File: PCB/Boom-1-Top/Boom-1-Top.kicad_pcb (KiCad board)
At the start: 2 copper layers, 345 x 165 mm, 493 parts, among them J1 DEBUG, J10 MCLRCap, J10 PIC_DEBUG, J11 MCLRCap, J11 PIC_DEBUG, J12 MCLRCap, J12 PIC_DEBUG, J13 MCLRCap, J13 PIC_DEBUG, J14 MCLRCap, J14 PIC_DEBUG, J2 MIDI IN, J3 MIDI OUT, J37 Osc1Conn, J38 Osc2Conn, J39 SubNoiseConn, J4 MCLRCap, J4 PIC_DEBUG, J40 FiltConn2, J41 EnvGenConn2, J42 EnvGenConn1, J43 FXConn1, J44 FiltConn1, J45 FXConn2, J46 EnvGenConn3, J5 MCLRCap, J5 PIC_DEBUG, J6 MCLRCap, J6 PIC_DEBUG, J7 MCLRCap, J7 PIC_DEBUG, J8 MCLRCap, J8 PIC_DEBUG, J9 MCLRCap, J9 PIC_DEBUG, SW1 Rotary_Encoder, SW10 Rotary_Encoder, SW11 Rotary_Encoder, SW12 Rotary_Encoder, SW13 Rotary_Encoder, SW14 Rotary_Encoder, SW15 Rotary_Encoder_Switch, SW16 Rotary_Encoder_Switch, SW17 Rotary_Encoder, SW18 Rotary_Encoder, SW19 Rotary_Encoder, SW2 Rotary_Encoder, SW20 Rotary_Encoder, SW21 Rotary_Encoder, SW22 Rotary_Encoder, SW23 Rotary_Encoder, SW24 Rotary_Encoder, SW25 Rotary_Encoder, SW26 Rotary_Encoder, SW27 Rotary_Encoder, SW28 Rotary_Encoder_Switch, SW29 Rotary_Encoder, SW3 Rotary_Encoder, SW30 Rotary_Encoder, SW31 Rotary_Encoder, SW32 Rotary_Encoder, SW33 Rotary_Encoder, SW34 Rotary_Encoder, SW35 Rotary_Encoder, SW36 Rotary_Encoder, SW37 Rotary_Encoder, SW38 Rotary_Encoder, SW39 Rotary_Encoder, SW4 Rotary_Encoder, SW40 Rotary_Encoder, SW41 Reset, SW42 Reset, SW43 Reset, SW44 Reset, SW45 Reset, SW46 Reset, SW47 Reset, SW48 Reset, SW49 Reset, SW5 Rotary_Encoder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

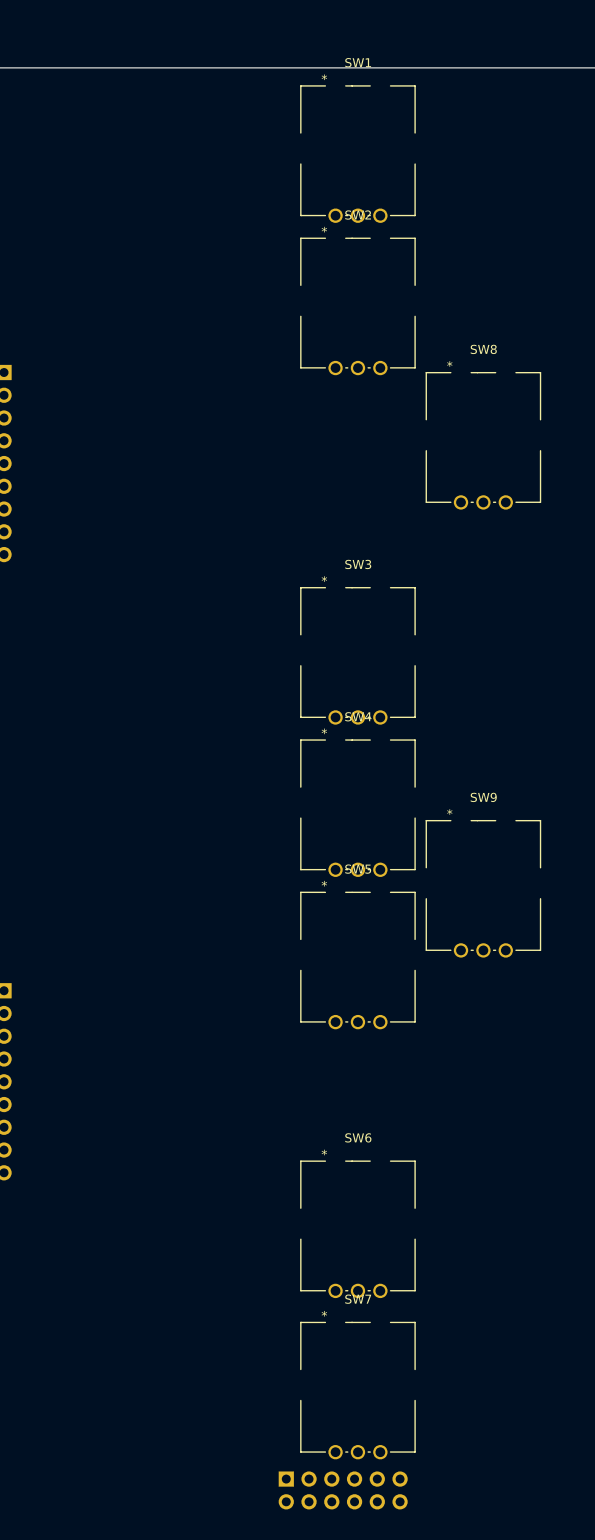
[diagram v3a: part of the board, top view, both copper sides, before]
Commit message: locked headers
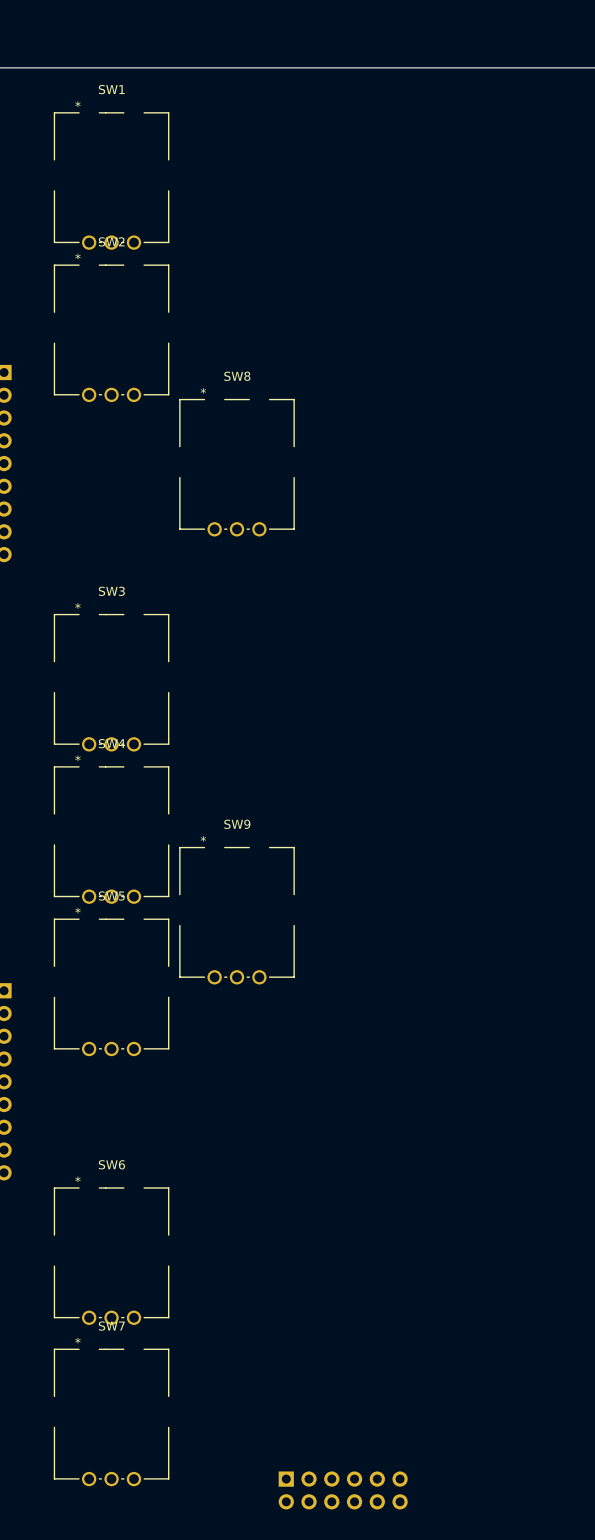
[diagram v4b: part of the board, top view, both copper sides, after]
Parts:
- moved SW1 27.7 mm to (48.5, 35.0)
- moved SW2 27.7 mm to (48.5, 52.0)
- moved SW3 27.7 mm to (48.5, 91.0)
- moved SW4 27.7 mm to (48.5, 108.0)
- moved SW5 27.7 mm to (48.5, 125.0)
- moved SW6 27.7 mm to (48.5, 155.0)
- moved SW7 27.7 mm to (48.5, 173.0)
- moved SW8 27.7 mm to (62.5, 67.0)
- moved SW9 27.7 mm to (62.5, 117.0)
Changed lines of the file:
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@@
   )
   (module PEC11R:PEC11R-4x15F-N0024 (layer F.Cu)
-    (at 90 114)
+    (at 62.5 117)
     (fp_text reference SW9 (at 2.54 -2.54) (layer F.SilkS)
       (effects (font (size 1 1) (thickness 0.15)))
@@
   )
   (module PEC11R:PEC11R-4x15F-N0024 (layer F.Cu)
-    (at 90 64)
+    (at 62.5 67)
     (fp_text reference SW8 (at 2.54 -2.54) (layer F.SilkS)
       (effects (font (size 1 1) (thickness 0.15)))
@@
   )
   (module PEC11R:PEC11R-4x15F-N0024 (layer F.Cu)
-    (at 76 170)
+    (at 48.5 173)
     (fp_text reference SW7 (at 2.54 -2.54) (layer F.SilkS)
       (effects (font (size 1 1) (thickness 0.15)))
@@
   )
   (module PEC11R:PEC11R-4x15F-N0024 (layer F.Cu)
-    (at 76 152)
+    (at 48.5 155)
     (fp_text reference SW6 (at 2.54 -2.54) (layer F.SilkS)
       (effects (font (size 1 1) (thickness 0.15)))
@@
   )
   (module PEC11R:PEC11R-4x15F-N0024 (layer F.Cu)
-    (at 76 122)
+    (at 48.5 125)
     (fp_text reference SW5 (at 2.54 -2.54) (layer F.SilkS)
       (effects (font (size 1 1) (thickness 0.15)))
@@
   )
   (module PEC11R:PEC11R-4x15F-N0024 (layer F.Cu)
-    (at 76 105)
+    (at 48.5 108)
     (fp_text reference SW4 (at 2.54 -2.54) (layer F.SilkS)
       (effects (font (size 1 1) (thickness 0.15)))
@@
   )
   (module PEC11R:PEC11R-4x15F-N0024 (layer F.Cu)
-    (at 76 88)
+    (at 48.5 91)
     (fp_text reference SW3 (at 2.54 -2.54) (layer F.SilkS)
       (effects (font (size 1 1) (thickness 0.15)))
@@
   )
   (module PEC11R:PEC11R-4x15F-N0024 (layer F.Cu)
-    (at 76 49)
+    (at 48.5 52)
     (fp_text reference SW2 (at 2.54 -2.54) (layer F.SilkS)
       (effects (font (size 1 1) (thickness 0.15)))
@@
   )
   (module PEC11R:PEC11R-4x15F-N0024 (layer F.Cu)
-    (at 76 32)
+    (at 48.5 35)
     (fp_text reference SW1 (at 2.54 -2.54) (layer F.SilkS)
       (effects (font (size 1 1) (thickness 0.15)))
@@
     )
   )
-  (module Connector_PinHeader_2.54mm:PinHeader_2x09_P2.54mm_Vertical (layer B.Cu)
+  (module Connector_PinHeader_2.54mm:PinHeader_2x09_P2.54mm_Vertical locked (layer B.Cu)
     (at 370.5 149.5 180)
     (descr "Through hole straight pin header, 2x09, 2.54mm pitch, double rows")
@@
     )
   )
-  (module Connector_PinHeader_2.54mm:PinHeader_2x05_P2.54mm_Vertical (layer B.Cu)
+  (module Connector_PinHeader_2.54mm:PinHeader_2x05_P2.54mm_Vertical locked (layer B.Cu)
     (at 269 34.5 270)
     (descr "Through hole straight pin header, 2x05, 2.54mm pitch, double rows")
@@
     )
   )
-  (module Connector_PinHeader_2.54mm:PinHeader_2x04_P2.54mm_Vertical (layer B.Cu)
+  (module Connector_PinHeader_2.54mm:PinHeader_2x04_P2.54mm_Vertical locked (layer B.Cu)
     (at 129 34.5 270)
     (descr "Through hole straight pin header, 2x04, 2.54mm pitch, double rows")
@@
     )
   )
-  (module Connector_PinHeader_2.54mm:PinHeader_2x08_P2.54mm_Vertical (layer B.Cu)
+  (module Connector_PinHeader_2.54mm:PinHeader_2x08_P2.54mm_Vertical locked (layer B.Cu)
     (at 236.5 187.5 270)
     (descr "Through hole straight pin header, 2x08, 2.54mm pitch, double rows")
@@
     )
   )
-  (module Connector_PinHeader_2.54mm:PinHeader_2x09_P2.54mm_Vertical (layer B.Cu)
+  (module Connector_PinHeader_2.54mm:PinHeader_2x09_P2.54mm_Vertical locked (layer B.Cu)
     (at 370.5 57 180)
     (descr "Through hole straight pin header, 2x09, 2.54mm pitch, double rows")
@@
     )
   )
-  (module Connector_PinHeader_2.54mm:PinHeader_2x09_P2.54mm_Vertical (layer B.Cu)
+  (module Connector_PinHeader_2.54mm:PinHeader_2x09_P2.54mm_Vertical locked (layer B.Cu)
     (at 370.5 101 180)
     (descr "Through hole straight pin header, 2x09, 2.54mm pitch, double rows")
@@
     )
   )
-  (module Connector_PinHeader_2.54mm:PinHeader_2x12_P2.54mm_Vertical (layer B.Cu)
+  (module Connector_PinHeader_2.54mm:PinHeader_2x12_P2.54mm_Vertical locked (layer B.Cu)
     (at 148 187.5 270)
     (descr "Through hole straight pin header, 2x12, 2.54mm pitch, double rows")
@@
     )
   )
-  (module Connector_PinHeader_2.54mm:PinHeader_2x06_P2.54mm_Vertical (layer B.Cu)
+  (module Connector_PinHeader_2.54mm:PinHeader_2x06_P2.54mm_Vertical locked (layer B.Cu)
     (at 70.5 187.5 270)
     (descr "Through hole straight pin header, 2x06, 2.54mm pitch, double rows")
@@
     )
   )
-  (module Connector_PinHeader_2.54mm:PinHeader_2x09_P2.54mm_Vertical (layer B.Cu)
+  (module Connector_PinHeader_2.54mm:PinHeader_2x09_P2.54mm_Vertical locked (layer B.Cu)
     (at 39 133 180)
     (descr "Through hole straight pin header, 2x09, 2.54mm pitch, double rows")
@@
     )
   )
-  (module Connector_PinHeader_2.54mm:PinHeader_2x09_P2.54mm_Vertical (layer B.Cu)
+  (module Connector_PinHeader_2.54mm:PinHeader_2x09_P2.54mm_Vertical locked (layer B.Cu)
     (at 39 64 180)
     (descr "Through hole straight pin header, 2x09, 2.54mm pitch, double rows")

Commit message: pcb layout for encoders
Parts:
- moved SW38 54.1 mm to (353.5, 120.0)
- moved SW37 51.1 mm to (335.5, 106.0)
- moved SW19 46.9 mm to (157.0, 167.0)
- moved SW34 42.3 mm to (311.5, 106.0)
- moved SW39 38.8 mm to (324.5, 159.0)
- moved SW40 37.7 mm to (324.5, 53.0)
- moved SW31 33.5 mm to (287.5, 106.0)
- moved SW28 30.6 mm to (269.5, 92.0)
- moved SW35 30.2 mm to (300.5, 159.0)
- moved SW36 28.8 mm to (300.5, 53.0)
- moved SW27 25.6 mm to (217.0, 139.0)
- moved SW26 22.6 mm to (217.0, 74.0)
- moved SW32 21.9 mm to (276.5, 159.0)
- moved SW33 19.9 mm to (276.5, 53.0)
- moved SW23 18.4 mm to (193.0, 139.0)
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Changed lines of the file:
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@@
   (general
     (thickness 1.6)
-    (drawings 4)
+    (drawings 7)
     (tracks 0)
     (zones 0)
@@
   )
   (module PEC11R:PEC11R-4x15F-N0024 (layer F.Cu)
-    (at 287 57)
+    (at 324.5 53)
     (fp_text reference SW40 (at 2.54 -2.54) (layer F.SilkS)
       (effects (font (size 1 1) (thickness 0.15)))
@@
   )
   (module PEC11R:PEC11R-4x15F-N0024 (layer F.Cu)
-    (at 287 169)
+    (at 324.5 159)
     (fp_text reference SW39 (at 2.54 -2.54) (layer F.SilkS)
       (effects (font (size 1 1) (thickness 0.15)))
@@
   )
   (module PEC11R:PEC11R-4x15F-N0024 (layer F.Cu)
-    (at 300 128)
+    (at 353.5 120)
     (fp_text reference SW38 (at 2.54 -2.54) (layer F.SilkS)
       (effects (font (size 1 1) (thickness 0.15)))
@@
   )
   (module PEC11R:PEC11R-4x15F-N0024 (layer F.Cu)
-    (at 285 114)
+    (at 335.5 106)
     (fp_text reference SW37 (at 2.54 -2.54) (layer F.SilkS)
       (effects (font (size 1 1) (thickness 0.15)))
@@
   )
   (module PEC11R:PEC11R-4x15F-N0024 (layer F.Cu)
-    (at 272 57)
+    (at 300.5 53)
     (fp_text reference SW36 (at 2.54 -2.54) (layer F.SilkS)
       (effects (font (size 1 1) (thickness 0.15)))
@@
   )
   (module PEC11R:PEC11R-4x15F-N0024 (layer F.Cu)
-    (at 272 169)
+    (at 300.5 159)
     (fp_text reference SW35 (at 2.54 -2.54) (layer F.SilkS)
       (effects (font (size 1 1) (thickness 0.15)))
@@
   )
   (module PEC11R:PEC11R-4x15F-N0024 (layer F.Cu)
-    (at 270 114)
+    (at 311.5 106)
     (fp_text reference SW34 (at 2.54 -2.54) (layer F.SilkS)
       (effects (font (size 1 1) (thickness 0.15)))
@@
   )
   (module PEC11R:PEC11R-4x15F-N0024 (layer F.Cu)
-    (at 257 57)
+    (at 276.5 53)
     (fp_text reference SW33 (at 2.54 -2.54) (layer F.SilkS)
       (effects (font (size 1 1) (thickness 0.15)))
@@
   )
   (module PEC11R:PEC11R-4x15F-N0024 (layer F.Cu)
-    (at 257 169)
+    (at 276.5 159)
     (fp_text reference SW32 (at 2.54 -2.54) (layer F.SilkS)
       (effects (font (size 1 1) (thickness 0.15)))
@@
   )
   (module PEC11R:PEC11R-4x15F-N0024 (layer F.Cu)
-    (at 255 114)
+    (at 287.5 106)
     (fp_text reference SW31 (at 2.54 -2.54) (layer F.SilkS)
       (effects (font (size 1 1) (thickness 0.15)))
@@
   )
   (module PEC11R:PEC11R-4x15F-N0024 (layer F.Cu)
-    (at 242 57)
+    (at 252.5 53)
     (fp_text reference SW30 (at 2.54 -2.54) (layer F.SilkS)
       (effects (font (size 1 1) (thickness 0.15)))
@@
   )
   (module PEC11R:PEC11R-4x15F-N0024 (layer F.Cu)
-    (at 242 169)
+    (at 252.5 159)
     (fp_text reference SW29 (at 2.54 -2.54) (layer F.SilkS)
       (effects (font (size 1 1) (thickness 0.15)))
@@
   )
   (module PEC11R:PEC11R-4x15F-S0024 (layer F.Cu)
-    (at 240 100)
+    (at 269.5 92)
     (fp_text reference SW28 (at 2.54 -2.54) (layer F.SilkS)
       (effects (font (size 1 1) (thickness 0.15)))
@@
   )
   (module PEC11R:PEC11R-4x15F-N0024 (layer F.Cu)
-    (at 195 152)
+    (at 217 139)
     (fp_text reference SW27 (at 2.54 -2.54) (layer F.SilkS)
       (effects (font (size 1 1) (thickness 0.15)))
@@
   )
   (module PEC11R:PEC11R-4x15F-N0024 (layer F.Cu)
-    (at 195 79)
+    (at 217 74)
     (fp_text reference SW26 (at 2.54 -2.54) (layer F.SilkS)
       (effects (font (size 1 1) (thickness 0.15)))
@@
   )
   (module PEC11R:PEC11R-4x15F-N0024 (layer F.Cu)
-    (at 202 107)
+    (at 204 105.5)
     (fp_text reference SW25 (at 2.54 -2.54) (layer F.SilkS)
       (effects (font (size 1 1) (thickness 0.15)))
@@
   )
   (module PEC11R:PEC11R-4x15F-N0024 (layer F.Cu)
-    (at 202 53)
+    (at 204 42.5)
     (fp_text reference SW24 (at 2.54 -2.54) (layer F.SilkS)
       (effects (font (size 1 1) (thickness 0.15)))
@@
   )
   (module PEC11R:PEC11R-4x15F-N0024 (layer F.Cu)
-    (at 180 152)
+    (at 193 139)
     (fp_text reference SW23 (at 2.54 -2.54) (layer F.SilkS)
       (effects (font (size 1 1) (thickness 0.15)))
@@
   )
   (module PEC11R:PEC11R-4x15F-N0024 (layer F.Cu)
-    (at 180 79)
+    (at 193 74)
     (fp_text reference SW22 (at 2.54 -2.54) (layer F.SilkS)
       (effects (font (size 1 1) (thickness 0.15)))
@@
   )
   (module PEC11R:PEC11R-4x15F-N0024 (layer F.Cu)
-    (at 165 152)
+    (at 169 139)
     (fp_text reference SW21 (at 2.54 -2.54) (layer F.SilkS)
       (effects (font (size 1 1) (thickness 0.15)))
@@
   )
   (module PEC11R:PEC11R-4x15F-N0024 (layer F.Cu)
-    (at 165 79)
+    (at 169 74)
     (fp_text reference SW20 (at 2.54 -2.54) (layer F.SilkS)
       (effects (font (size 1 1) (thickness 0.15)))
@@
   )
   (module PEC11R:PEC11R-4x15F-N0024 (layer F.Cu)
-    (at 203 176)
+    (at 157 167)
     (fp_text reference SW19 (at 2.54 -2.54) (layer F.SilkS)
       (effects (font (size 1 1) (thickness 0.15)))
@@
   )
   (module PEC11R:PEC11R-4x15F-N0024 (layer F.Cu)
-    (at 171 106)
+    (at 156.5 105.5)
     (fp_text reference SW18 (at 2.54 -2.54) (layer F.SilkS)
       (effects (font (size 1 1) (thickness 0.15)))
@@
   )
   (module PEC11R:PEC11R-4x15F-N0024 (layer F.Cu)
-    (at 171 53)
+    (at 157 42.5)
     (fp_text reference SW17 (at 2.54 -2.54) (layer F.SilkS)
       (effects (font (size 1 1) (thickness 0.15)))
@@
   )
   (module PEC11R:PEC11R-4x15F-S0024 (layer F.Cu)
-    (at 150 152)
+    (at 145 139)
     (fp_text reference SW16 (at 2.54 -2.54) (layer F.SilkS)
       (effects (font (size 1 1) (thickness 0.15)))
@@
   )
   (module PEC11R:PEC11R-4x15F-S0024 (layer F.Cu)
-    (at 150 79)
+    (at 145 74)
     (fp_text reference SW15 (at 2.54 -2.54) (layer F.SilkS)
       (effects (font (size 1 1) (thickness 0.15)))
@@
   )
   (module PEC11R:PEC11R-4x15F-N0024 (layer F.Cu)
-    (at 140 176)
+    (at 133 167)
     (fp_text reference SW14 (at 2.54 -2.54) (layer F.SilkS)
       (effects (font (size 1 1) (thickness 0.15)))
@@
   )
   (module PEC11R:PEC11R-4x15F-N0024 (layer F.Cu)
-    (at 140 106)
+    (at 133 105.5)
     (fp_text reference SW13 (at 2.54 -2.54) (layer F.SilkS)
       (effects (font (size 1 1) (thickness 0.15)))
@@
   )
   (module PEC11R:PEC11R-4x15F-N0024 (layer F.Cu)
-    (at 140 53)
+    (at 133 42.5)
     (fp_text reference SW12 (at 2.54 -2.54) (layer F.SilkS)
       (effects (font (size 1 1) (thickness 0.15)))
@@
   )
   (module PEC11R:PEC11R-4x15F-N0024 (layer F.Cu)
-    (at 115 70)
+    (at 99.5 70)
     (fp_text reference SW11 (at 2.54 -2.54) (layer F.SilkS)
       (effects (font (size 1 1) (thickness 0.15)))
@@
   )
   (module PEC11R:PEC11R-4x15F-N0024 (layer F.Cu)
-    (at 115 137)
+    (at 99.5 141.5)
     (fp_text reference SW10 (at 2.54 -2.54) (layer F.SilkS)
       (effects (font (size 1 1) (thickness 0.15)))
@@
   )
   (module PEC11R:PEC11R-4x15F-N0024 (layer F.Cu)
-    (at 62.5 117)
+    (at 66 112)
     (fp_text reference SW9 (at 2.54 -2.54) (layer F.SilkS)
       (effects (font (size 1 1) (thickness 0.15)))
@@
   )
   (module PEC11R:PEC11R-4x15F-N0024 (layer F.Cu)
-    (at 62.5 67)
+    (at 66 61)
     (fp_text reference SW8 (at 2.54 -2.54) (layer F.SilkS)
       (effects (font (size 1 1) (thickness 0.15)))
@@
   )
   (module PEC11R:PEC11R-4x15F-N0024 (layer F.Cu)
-    (at 48.5 173)
+    (at 48.5 177.5)
     (fp_text reference SW7 (at 2.54 -2.54) (layer F.SilkS)
       (effects (font (size 1 1) (thickness 0.15)))
@@
   )
   (module PEC11R:PEC11R-4x15F-N0024 (layer F.Cu)
-    (at 48.5 155)
+    (at 48.5 156)
     (fp_text reference SW6 (at 2.54 -2.54) (layer F.SilkS)
       (effects (font (size 1 1) (thickness 0.15)))
@@
   )
   (module PEC11R:PEC11R-4x15F-N0024 (layer F.Cu)
-    (at 48.5 125)
+    (at 48.5 126.5)
     (fp_text reference SW5 (at 2.54 -2.54) (layer F.SilkS)
       (effects (font (size 1 1) (thickness 0.15)))
@@
   )
   (module PEC11R:PEC11R-4x15F-N0024 (layer F.Cu)
-    (at 48.5 108)
+    (at 48.5 105.5)
     (fp_text reference SW4 (at 2.54 -2.54) (layer F.SilkS)
       (effects (font (size 1 1) (thickness 0.15)))
@@
   )
   (module PEC11R:PEC11R-4x15F-N0024 (layer F.Cu)
-    (at 48.5 91)
+    (at 48.5 83.5)
     (fp_text reference SW3 (at 2.54 -2.54) (layer F.SilkS)
       (effects (font (size 1 1) (thickness 0.15)))
@@
   )
   (module PEC11R:PEC11R-4x15F-N0024 (layer F.Cu)
-    (at 48.5 52)
+    (at 48.5 54.5)
     (fp_text reference SW2 (at 2.54 -2.54) (layer F.SilkS)
       (effects (font (size 1 1) (thickness 0.15)))
@@
   )
   (module PEC11R:PEC11R-4x15F-N0024 (layer F.Cu)
-    (at 48.5 35)
+    (at 48.5 33)
     (fp_text reference SW1 (at 2.54 -2.54) (layer F.SilkS)
       (effects (font (size 1 1) (thickness 0.15)))
@@
     )
   )
+  (target plus (at 202.5 30) (size 5) (width 0.05) (layer Edge.Cuts))
+  (target plus (at 375 112.5) (size 5) (width 0.05) (layer Edge.Cuts))
+  (target plus (at 30 112.5) (size 5) (width 0.05) (layer Edge.Cuts))
   (gr_line (start 30 195) (end 30 30) (layer Edge.Cuts) (width 0.05))
   (gr_line (start 375 195) (end 30 195) (layer Edge.Cuts) (width 0.05))

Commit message: started pic layout
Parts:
- moved U2 489.3 mm to (71.0, 41.5)
- moved U12 387.3 mm to (72.0, 171.5)
- moved U11 374.3 mm to (84.0, 115.5)
- moved J1 355.4 mm to (237.0, 122.5)
- moved U21 353.3 mm to (237.5, 113.0)
- moved U1 170.9 mm to (251.0, 127.5)
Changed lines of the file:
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@@
   )
   (module Package_TO_SOT_SMD:SOT-223-3_TabPin2 (layer F.Cu)
-    (at 500.35 349.13)
+    (at 237.5 113)
     (descr "module CMS SOT223 4 pins")
     (tags "CMS SOT")
@@
   )
   (module Connector_PinHeader_1.27mm:PinHeader_2x05_P1.27mm_Vertical_SMD (layer F.Cu)
-    (at 535.53 315.41)
+    (at 237 122.5)
     (descr "surface-mounted straight pin header, 2x05, 1.27mm pitch, double rows")
     (tags "Surface mounted pin header SMD 2x05 1.27mm double row")
@@
   )
   (module Package_SO:SSOP-28_5.3x10.2mm_P0.65mm (layer F.Cu)
-    (at 432.79 312.22)
+    (at 72 171.5)
     (descr "28-Lead Plastic Shrink Small Outline (SS)-5.30 mm Body [SSOP] (see Microchip Packaging Specification 00000049BS.pdf)")
     (tags "SSOP 0.65")
@@
   )
   (module Package_SO:SSOP-28_5.3x10.2mm_P0.65mm (layer F.Cu)
-    (at 402.01 312.95)
+    (at 84 115.5)
     (descr "28-Lead Plastic Shrink Small Outline (SS)-5.30 mm Body [SSOP] (see Microchip Packaging Specification 00000049BS.pdf)")
     (tags "SSOP 0.65")
@@
   )
   (module Package_SO:SSOP-28_5.3x10.2mm_P0.65mm (layer F.Cu)
-    (at 525.26 223.42)
+    (at 71 41.5)
     (descr "28-Lead Plastic Shrink Small Outline (SS)-5.30 mm Body [SSOP] (see Microchip Packaging Specification 00000049BS.pdf)")
     (tags "SSOP 0.65")
@@
   )
   (module Package_QFP:LQFP-100_14x14mm_P0.5mm (layer F.Cu)
-    (at 390.26 226.64)
+    (at 251 127.5)
     (descr "LQFP, 100 Pin (https://www.nxp.com/docs/en/package-information/SOT407-1.pdf), generated with kicad-footprint-generator ipc_gullwing_generator.py")
     (tags "LQFP QFP")

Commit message: Rotary encoder layout near final
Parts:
- moved SW37 7.02 mm to (328.5, 105.5)
- moved SW28 5.14 mm to (264.5, 90.8)
- moved SW34 3.04 mm to (308.5, 105.5)
- moved SW29 3.00 mm to (252.5, 156.0)
- moved SW32 3.00 mm to (276.5, 156.0)
- moved SW35 3.00 mm to (300.5, 156.0)
- moved SW39 3.00 mm to (324.5, 156.0)
- moved SW16 2.50 mm to (145.0, 136.5)
- moved SW21 2.50 mm to (169.0, 136.5)
- moved SW23 2.50 mm to (193.0, 136.5)
- moved SW27 2.50 mm to (217.0, 136.5)
- moved SW30 2.05 mm to (252.6, 55.0)
- moved SW33 2.05 mm to (276.6, 55.0)
- moved SW36 2.05 mm to (300.6, 55.0)
- moved SW40 2.05 mm to (324.6, 55.0)
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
